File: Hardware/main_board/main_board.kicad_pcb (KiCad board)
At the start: 6 copper layers, 95.4 x 36.1 mm, 237 parts, among them J1 BATT, J2 LCD, J3 BACK_LIGHT, J4 SD, J5 NFC, J6 EXT1, J7 EXT0, J8 USB_C, Q1 DMN313DLT, SW1 OK, SW2 BACK, SW3 RIGHT, SW4 LEFT, SW5 UP, SW6 DOWN, T1 B0310J50100AHF, U1 STM32WB55RGVx, U10 BGS13S4N9E6327XTSA1, U11 NC7SZ32M5X, U12 LP5562TMX, U2 BQ27220YZFR, U3 BQ25896RTWR, U4 RS3221-3.3YF3, U5 LM66100DCK, U6 LM3281YFQR, U7 LM3281YFQR, U8 CC1101RGP, U9 BGS13S4N9E6327XTSA1, Y1 32MHz, Y2 32.768K, Y3 26MHz

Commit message: silkscreen: start edit the silkscreens
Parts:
- moved TP1 0.15 mm to (143.6, 106.5)
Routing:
- net /LCD/LCD_LED: track 38.7 -> 33.8 mm
- net GND: vias 42 -> 46
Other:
- board text added: "1"
- board text added: "2"
- board text added: "3"
- board text added: "4"
- board text added: "5"
- board text added: "6"
- board text added: "NTC"
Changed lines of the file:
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@@
 	(footprint "TestPoint:TestPoint_Pad_D1.0mm"
 		(layer "B.Cu")
-		(at 143.71 106.480001 180)
+		(at 143.56 106.480001 180)
 		(descr "SMD pad as test Point, diameter 1.0mm")
 		(tags "test point SMD pad")
@@
 		)
 	)
+	(gr_poly
+		(pts
+			(xy 177.671975 121.88) (xy 176.671978 121.88) (xy 177.171977 121.380001)
+		)
+		(stroke
+			(width 0.15)
+			(type solid)
+		)
+		(fill solid)
+		(layer "F.SilkS")
+	)
 	(gr_line
 		(start 159.901976 84.738559)
@@
 		)
 	)
+	(gr_text "1"
+		(at 127.030715 123.875 0)
+		(layer "F.Cu")
+		(effects
+			(font
+				(size 1.5 1.5)
+				(thickness 0.3)
+				(bold yes)
+			)
+			(justify left bottom)
+		)
+	)
+	(gr_text "2"
+		(at 128.375 123.875 0)
+		(layer "In1.Cu")
+		(effects
+			(font
+				(size 1.5 1.5)
+				(thickness 0.3)
+				(bold yes)
+			)
+			(justify left bottom)
+		)
+	)
+	(gr_text "3"
+		(at 129.719285 123.875 0)
+		(layer "In2.Cu")
+		(effects
+			(font
+				(size 1.5 1.5)
+				(thickness 0.3)
+				(bold yes)
+			)
+			(justify left bottom)
+		)
+	)
+	(gr_text "4"
+		(at 132.93643 123.875 0)
+		(layer "In3.Cu")
+		(effects
+			(font
+				(size 1.5 1.5)
+				(thickness 0.3)
+				(bold yes)
+			)
+			(justify left bottom mirror)
+		)
+	)
+	(gr_text "5"
+		(at 134.280715 123.875 0)
+		(layer "In4.Cu")
+		(effects
+			(font
+				(size 1.5 1.5)
+				(thickness 0.3)
+				(bold yes)
+			)
+			(justify left bottom mirror)
+		)
+	)
+	(gr_text "6"
+		(at 135.625 123.875 0)
+		(layer "B.Cu")
+		(effects
+			(font
+				(size 1.5 1.5)
+				(thickness 0.3)
+				(bold yes)
+			)
+			(justify left bottom mirror)
+		)
+	)
+	(gr_text "NTC"
+		(at 177.171976 122.09 0)
+		(layer "F.SilkS")
+		(effects
+			(font
+				(size 1 1)
+				(thickness 0.15)
+			)
+			(justify top)
+		)
+	)
 	(segment
 		(start 155.7 96.231924)
@@
 	)
 	(via
+		(at 126.53 113.54)
+		(size 0.3778)
+		(drill 0.2)
+		(layers "F.Cu" "B.Cu")
+		(free yes)
+		(net 3)
+	)
+	(via
 		(at 157.83 101.49)
 		(size 0.3778)
@@
 	)
 	(via
+		(at 146.63 103.13)
+		(size 0.3778)
+		(drill 0.2)
+		(layers "F.Cu" "B.Cu")
+		(free yes)
+		(net 3)
+	)
+	(via
 		(at 170.97 109)
 		(size 0.3778)
@@
 	)
 	(via
-		(at 147.86 121.3)
-		(size 0.5)
-		(drill 0.3)
+		(at 153.97 119.19)
+		(size 0.3778)
+		(drill 0.2)
 		(layers "F.Cu" "B.Cu")
 		(free yes)
@@
 	)
 	(via
+		(at 141.78 109.22)
+		(size 0.3778)
+		(drill 0.2)
+		(layers "F.Cu" "B.Cu")
+		(free yes)
+		(net 3)
+	)
+	(via
 		(at 156.411976 99.048559)
 		(size 0.3778)
@@
 	)
 	(via
-		(at 135.81 122.21)
+		(at 135.97 120.89)
 		(size 0.5)
 		(drill 0.3)
@@
 	)
 	(via
+		(at 143.67 105.66)
+		(size 0.3778)
+		(drill 0.2)
+		(layers "F.Cu" "B.Cu")
+		(free yes)
+		(net 3)
+	)
+	(via
 		(at 156.381976 101.038559)
 		(size 0.3778)
@@
 	)
 	(segment
-		(start 135.24 108.47)
-		(end 138.41 108.47)
+		(start 139.7212 108.9388)
+		(end 145.5 103.16)
 		(width 0.2032)
 		(layer "B.Cu")
@@
 	)
 	(segment
-		(start 139.7212 108.9388)
-		(end 145.5 103.16)
+		(start 133.661976 108.648559)
+		(end 135.061441 108.648559)
 		(width 0.2032)
 		(layer "B.Cu")
@@
 	)
 	(segment
-		(start 133.661976 108.648559)
-		(end 135.061441 108.648559)
+		(start 138.8788 108.9388)
+		(end 139.7212 108.9388)
 		(width 0.2032)
 		(layer "B.Cu")
@@
 	)
 	(segment
-		(start 138.8788 108.9388)
-		(end 139.7212 108.9388)
+		(start 135.24 108.47)
+		(end 138.41 108.47)
 		(width 0.2032)
 		(layer "B.Cu")
@@
 	)
 	(segment
+		(start 143.56 106.480001)
+		(end 145.031976 106.480001)
+		(width 0.2032)
+		(layer "B.Cu")
+		(net 157)
+	)
+	(segment
 		(start 165.8575 116.2175)
 		(end 165.8575 116.666624)
@@
 	)
 	(segment
-		(start 143.71 106.480001)
-		(end 145.031976 106.480001)
-		(width 0.2032)
-		(layer "B.Cu")
-		(net 157)
-	)
-	(segment
 		(start 114.980978 120.261923)
 		(end 114.980978 119.774424)
@@
 	)
 	(segment
-		(start 162.74 122.81)
-		(end 164.58 120.97)
-		(width 0.508)
-		(layer "In3.Cu")
-		(net 172)
-	)
-	(segment
-		(start 135.571512 122.81)
-		(end 162.74 122.81)
-		(width 0.508)
-		(layer "In3.Cu")
-		(net 172)
-	)
-	(segment
-		(start 135.2171 122.44676)
-		(end 135.2171 122.455588)
-		(width 0.508)
-		(layer "In3.Cu")
-		(net 172)
-	)
-	(segment
-		(start 135.2171 122.455588)
-		(end 135.571512 122.81)
+		(start 133.884906 117.466624)
+		(end 164.58 117.466624)
 		(width 0.508)
 		(layer "In3.Cu")
@@
 	(segment
 		(start 132.060935 119.290595)
-		(end 135.2171 122.44676)
-		(width 0.508)
-		(layer "In3.Cu")
-		(net 172)
-	)
-	(segment
-		(start 164.58 120.97)
-		(end 164.58 117.466624)
+		(end 133.884906 117.466624)
 		(width 0.508)
 		(layer "In3.Cu")
@@
 	)
 	(zone
+		(net 0)
+		(net_name "")
+		(layers "F.Cu" "In1.Cu" "In2.Cu" "In3.Cu" "In4.Cu" "B.Cu")
+		(hatch edge 0.5)
+		(connect_pads
+			(clearance 0)
+		)
+		(min_thickness 0.25)
+		(filled_areas_thickness no)
+		(keepout
+			(tracks allowed)
+			(vias allowed)
+			(pads allowed)
+			(copperpour not_allowed)
+			(footprints allowed)
+		)
+		(fill
+			(thermal_gap 0.5)
+			(thermal_bridge_width 0.5)
+		)
+		(polygon
+			(pts
+				(xy 127.094285 124.125) (xy 135.594285 124.125) (xy 135.594285 121.625) (xy 127.094285 121.625)
+			)
+		)
+	)
+	(zone
 		(net 3)
 		(net_name "GND")
@@
 		)
 	)
+	(zone
+		(net 0)
+		(net_name "")
+		(layers "*.Mask")
+		(hatch edge 0.5)
+		(connect_pads
+			(clearance 0.1016)
+		)
+		(min_thickness 0.25)
+		(filled_areas_thickness no)
+		(fill yes
+			(thermal_gap 0.5)
+			(thermal_bridge_width 0.5)
+		)
+		(polygon
+			(pts
+				(xy 127.094285 121.625) (xy 127.094285 124.125) (xy 135.594285 124.125) (xy 135.594285 121.625)
+			)
+		)
+	)
 	(group ""
 		(members "048e3efe-b79a-44cc-b917-b631601fe3bb" "f1b9a218-ee50-415c-bce6-a34b4d77d02a")
@@
 		(members "17b71b92-ee64-4c28-9153-6b6d9b49c2a0" "cf6d0d25-a1b2-4383-911d-0bb30c3aab5b")
 	)
+	(group ""
+		(members "19e46f21-2a0c-497e-8ba7-df94bb00d366" "2e789cb3-3dcd-4d40-82c5-423cc5e9119f"
+			"359a7c8c-dd2e-4691-822e-3be476bf028f" "3f5870c5-ea67-42ad-b5aa-d0b626f0596f"
+			"8635445c-c8d1-4c70-9f5c-ad2b2cb28283" "a1187778-35c1-411b-87a5-f185abb89bcd"
+			"be09b38c-262f-45dc-947c-5a8b7ab2a9ad" "f5c6d2c6-541e-436b-9bc9-6c2253fa9a34"
+		)
+	)
+	(group ""
+		(members "0acd2d37-5dc5-4d1e-b103-f522034d819f" "ddf5bcaa-dbe1-4d42-8584-88c9cbc7f3e5")
+	)
 	(group "OUTLINE"

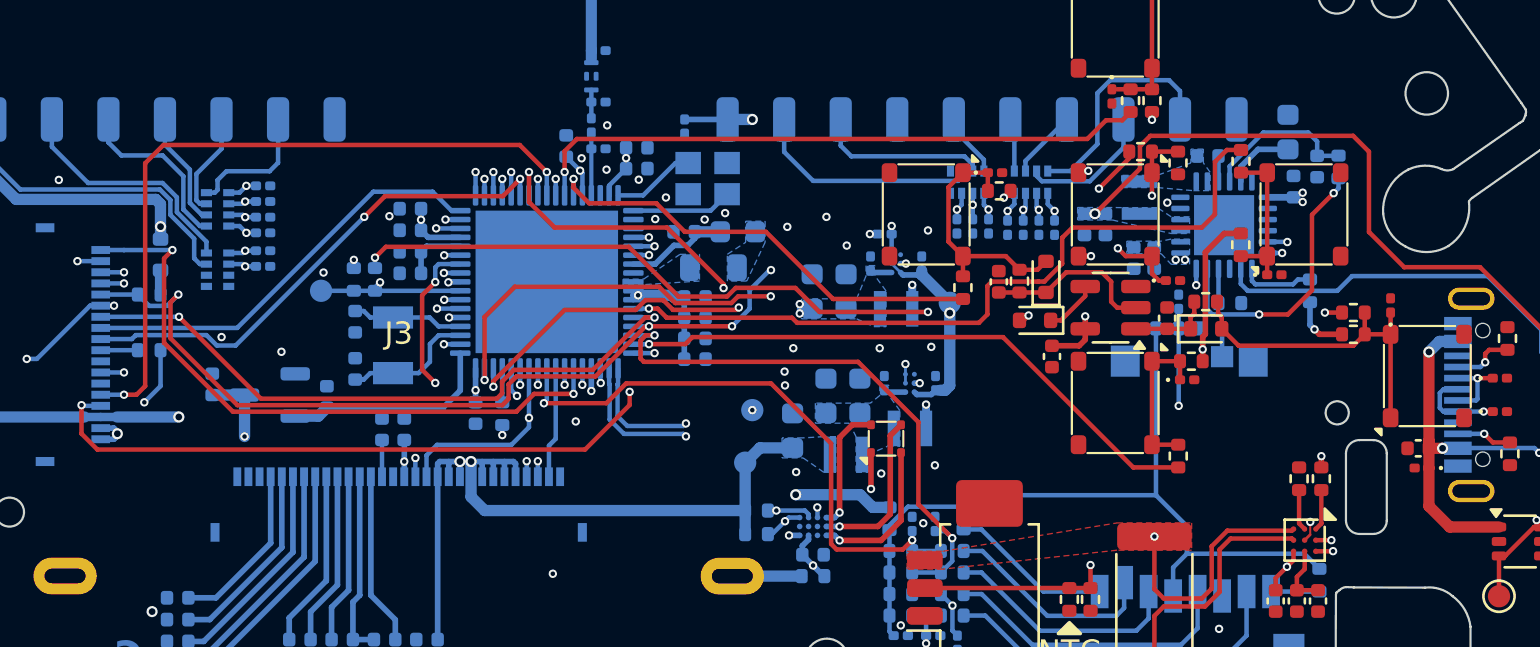
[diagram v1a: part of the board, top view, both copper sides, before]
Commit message: layout: change some routes
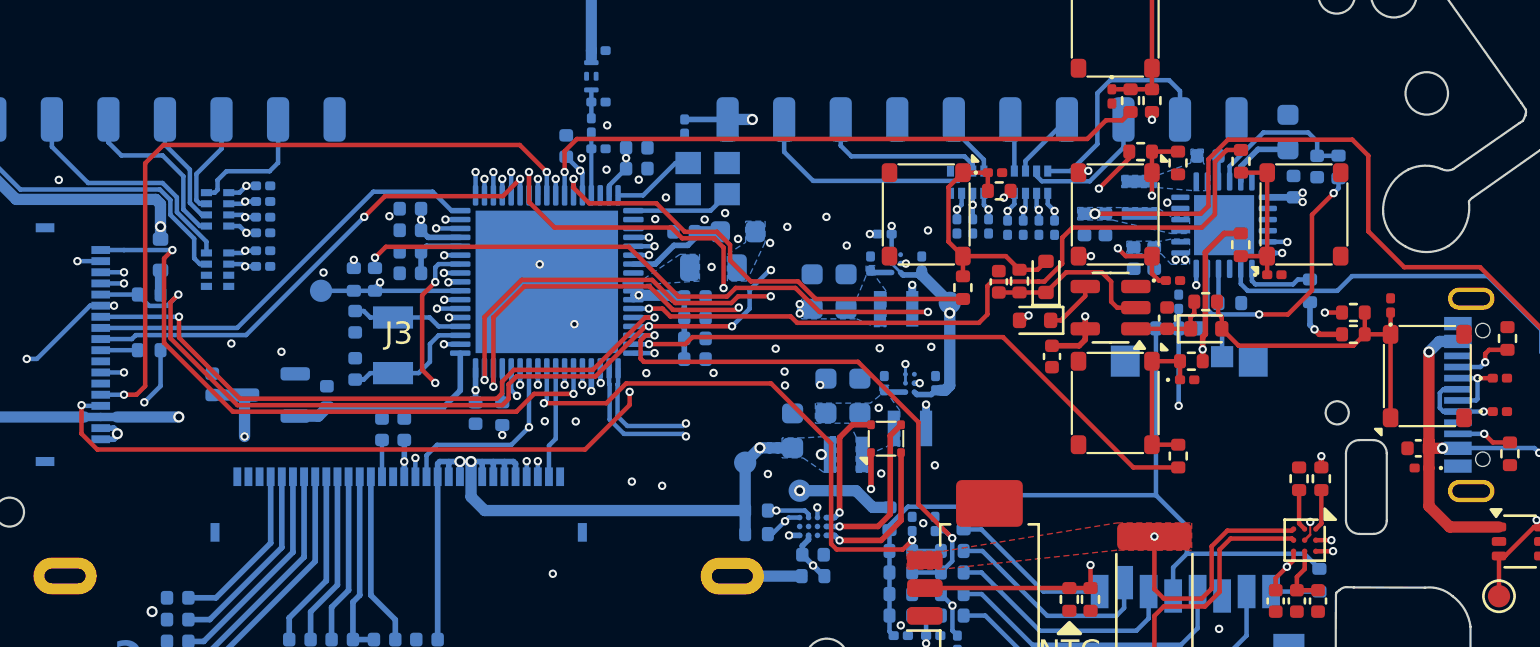
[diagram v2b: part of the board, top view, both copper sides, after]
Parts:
- moved TP21 4.20 mm to (165.1, 115.5)
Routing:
- net +3.3V_EXT: track 29.8 -> 27.2 mm, vias 5 -> 4
- net /MCU/UART1_TX: track 28.8 -> 31.0 mm
- net VUSB: track 118.2 -> 117.0 mm
- net /MCU/I2C_SCL: track 68.8 -> 69.7 mm
- net /MCU/RFID_OUT: track 29.2 -> 29.7 mm
- net +3.3V: vias 27 -> 29
- net GND: vias 46 -> 58

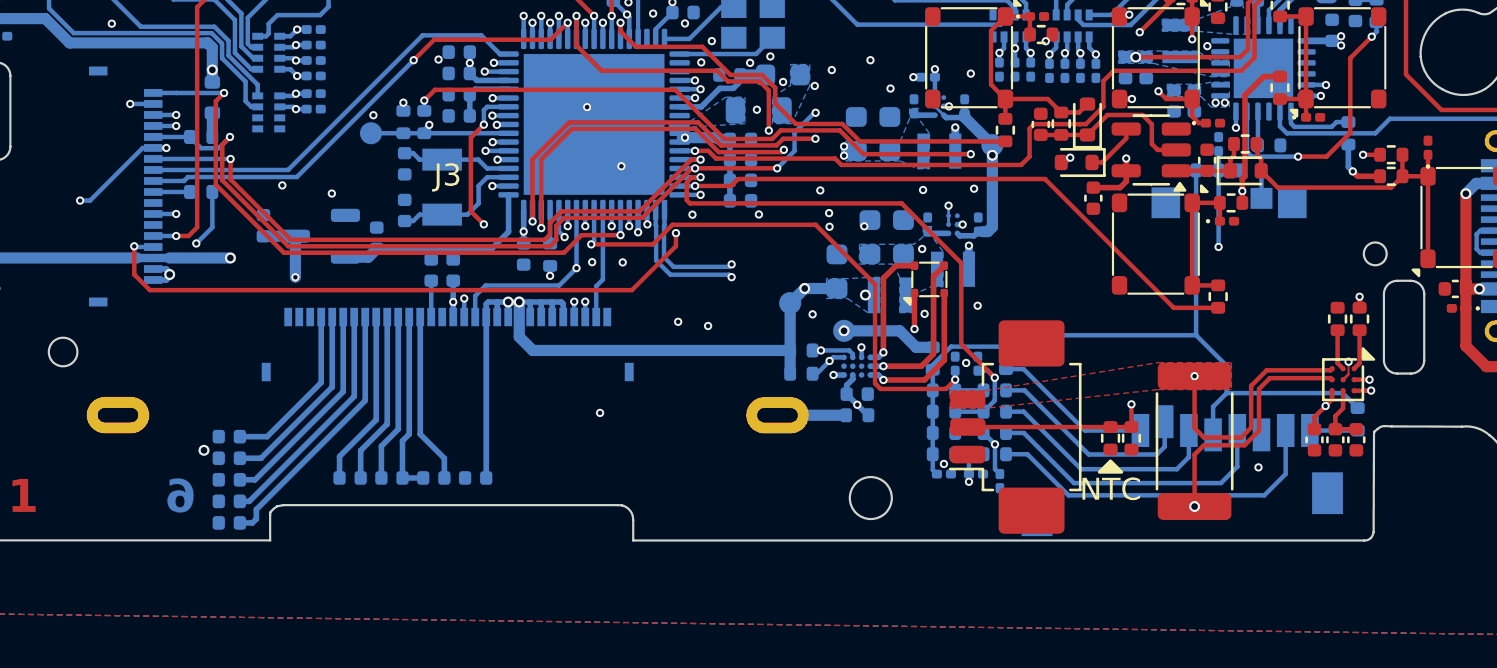
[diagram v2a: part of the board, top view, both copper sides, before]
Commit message: footprint: fix sd card
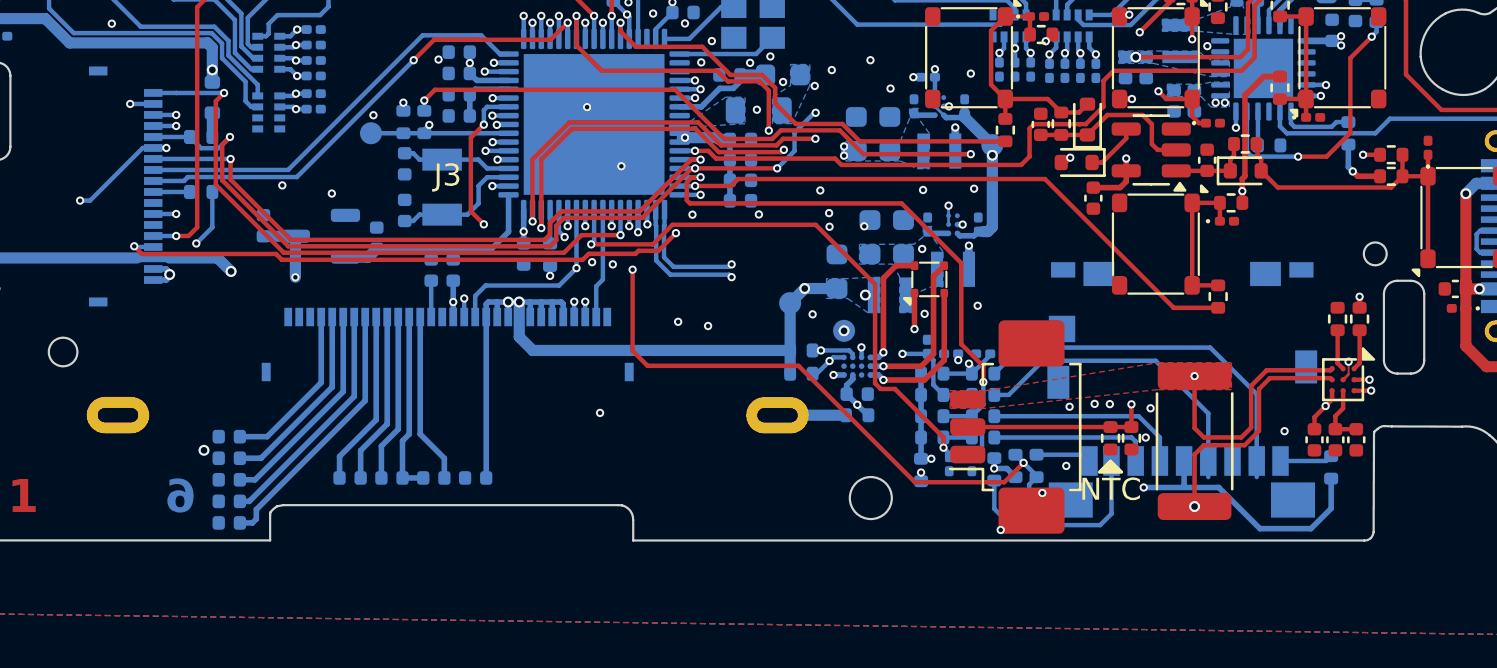
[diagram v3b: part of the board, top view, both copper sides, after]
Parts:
- J4: footprint Library:TF-101A-P3 -> Library:TF-SMD_TF-110
- moved D15 18.3 mm to (173.2, 122.9), turned to 180 degrees
- moved R48 16.6 mm to (173.8, 121.6), turned to 90 degrees
- moved R41 16.0 mm to (172.8, 121.6), turned to -90 degrees
- moved D13 6.94 mm to (168.8, 116.2), turned to 90 degrees
- moved D14 5.47 mm to (171.4, 116.5), turned to 180 degrees
- moved D16 5.47 mm to (169.9, 116.5), turned to 180 degrees
- moved R43 5.09 mm to (171.9, 121.8)
- moved R36 5.09 mm to (168.6, 121.8), turned to 90 degrees
- moved D12 4.57 mm to (170.9, 121.5), turned to -90 degrees
- moved D11 4.57 mm to (169.8, 121.5), turned to -90 degrees
- moved R47 3.70 mm to (171.4, 117.4)
- moved R40 3.70 mm to (169.1, 117.4)
- moved R42 2.50 mm to (187.2, 121.7), turned to -90 degrees
- moved R37 2.21 mm to (169.1, 120.3)
- moved R44 2.21 mm to (171.4, 120.3)
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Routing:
- net /MCU/SD_CD: track 34.8 -> 29.8 mm, vias 2 -> 3
- net +3.3V_EXT: track 27.2 -> 31.7 mm, vias 4 -> 5
- net Net-(D16-A1): track 36.8 -> 33.6 mm, vias 0 -> 4
- net Net-(J4-DAT2): track 7.27 -> 9.90 mm
- net /LCD/SPI_D_SCK: track 34.5 -> 32.1 mm
- net Net-(J4-DAT3/CD): track 9.70 -> 7.38 mm
- net /MCU/NFC_CS: track 35.7 -> 33.5 mm
- net /Buttons/RESET: track 31.1 -> 33.0 mm
- net Net-(J4-CMD): track 10.8 -> 8.99 mm
- net /LCD/SPI_D_MOSI: track 42.1 -> 43.4 mm
- net Net-(J4-DET): track 1.27 -> 2.52 mm
- net Net-(J4-DAT0): track 15.9 -> 17.1 mm
- net Net-(J4-CLK): track 13.4 -> 14.2 mm
- net /MCU/SD_CS: track 26.6 -> 27.4 mm
- net GND: vias 58 -> 64
